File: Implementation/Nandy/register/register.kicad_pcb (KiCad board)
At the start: 2 copper layers, 57.1 x 95.2 mm, 47 parts, among them J1 Conn_02x06_Odd_Even, J2 Conn_02x06_Odd_Even, J3 Conn_01x04_Male

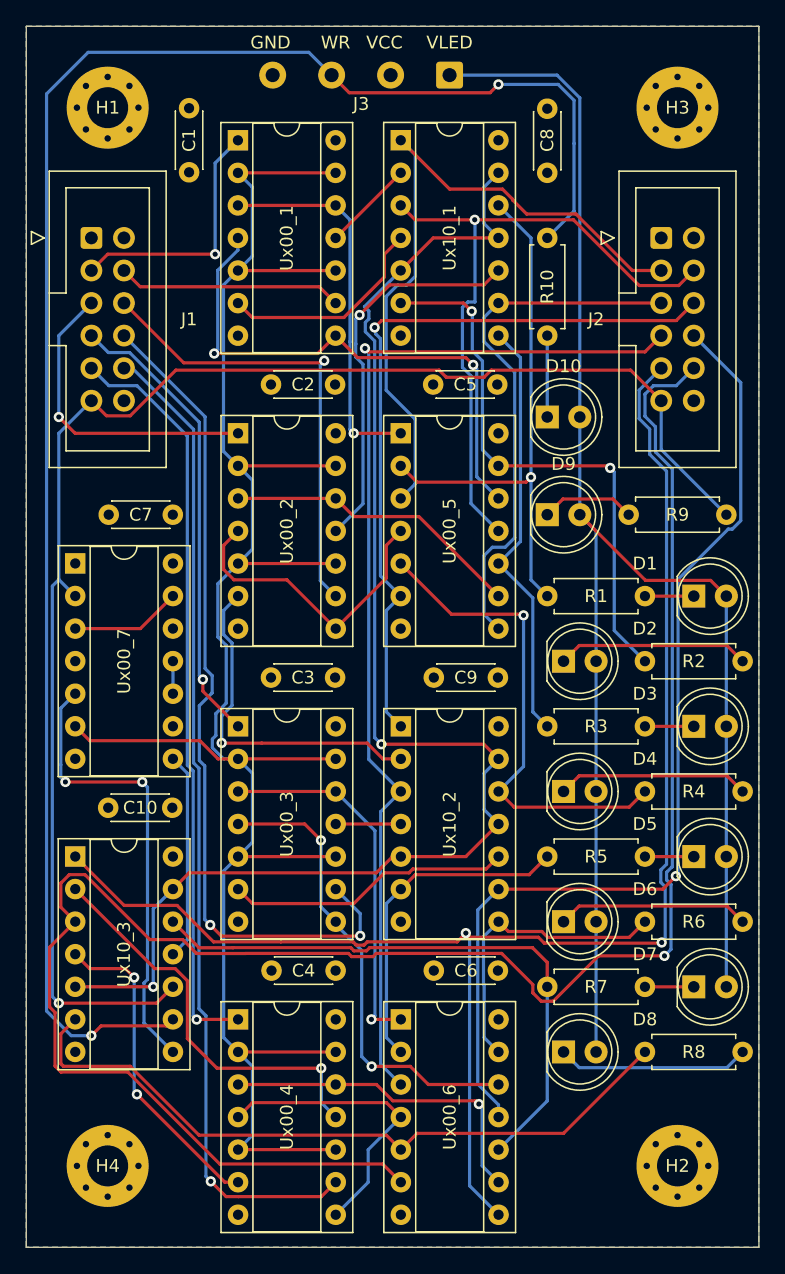
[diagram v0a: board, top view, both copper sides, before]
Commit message: Reworked Makefile with kikit
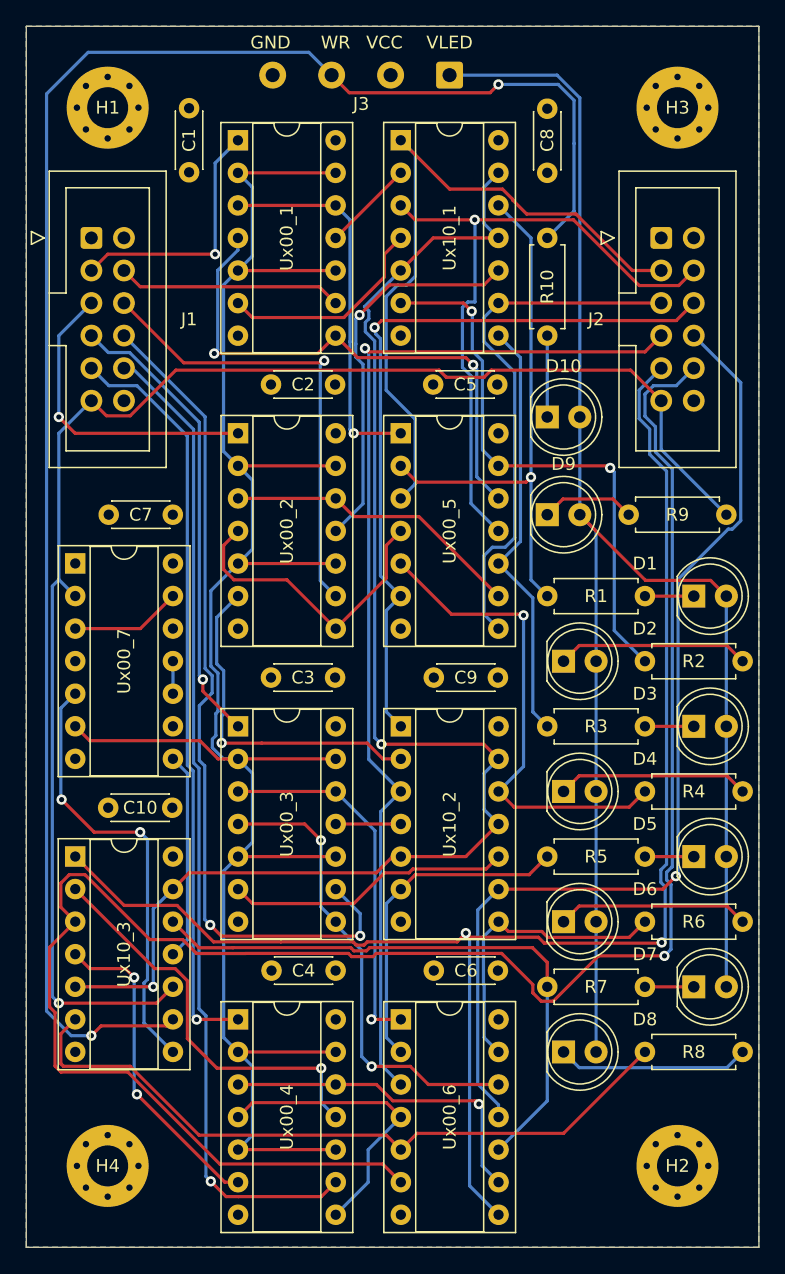
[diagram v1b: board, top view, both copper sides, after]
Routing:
- net /NTICK: track 35.8 -> 34.4 mm
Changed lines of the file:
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@@
       (plotinvisibletext false)
       (sketchpadsonfab false)
-      (subtractmaskfromsilk false)
+      (subtractmaskfromsilk true)
       (outputformat 1)
       (mirror false)
-      (drillshape 1)
+      (drillshape 0)
       (scaleselection 1)
       (outputdirectory "")
@@
     (fp_circle (center 13.8 0) (end 14.85 0)
       (stroke (width 0.1) (type solid)) (fill none) (layer "F.Fab"))
-    (pad "1" thru_hole roundrect (at 0 0 180) (size 2.1 2.1) (drill 1.1) (layers "*.Cu" "*.Mask") (roundrect_rratio 0.119048)
+    (pad "1" thru_hole roundrect (at 0 0 180) (size 2.1 2.1) (drill 1.1) (layers "*.Cu" "*.Mask") (roundrect_rratio 0.1190480952)
       (net 4 "+5VL") (pinfunction "Pin_1") (pintype "passive"))
     (pad "2" thru_hole circle (at 4.6 0 180) (size 2.1 2.1) (drill 1.1) (layers "*.Cu" "*.Mask")
@@
     (fp_line (start 5.72 17.8) (end -3.18 17.8)
       (stroke (width 0.1) (type solid)) (layer "F.Fab"))
-    (pad "1" thru_hole roundrect (at 0 0) (size 1.7 1.7) (drill 1) (layers "*.Cu" "*.Mask") (roundrect_rratio 0.147059)
+    (pad "1" thru_hole roundrect (at 0 0) (size 1.7 1.7) (drill 1) (layers "*.Cu" "*.Mask") (roundrect_rratio 0.1470588235)
       (net 1 "+5V") (pinfunction "Pin_1") (pintype "passive"))
     (pad "2" thru_hole circle (at 2.54 0) (size 1.7 1.7) (drill 1) (layers "*.Cu" "*.Mask")
@@
     (fp_line (start 5.72 17.8) (end -3.18 17.8)
       (stroke (width 0.1) (type solid)) (layer "F.Fab"))
-    (pad "1" thru_hole roundrect (at 0 0) (size 1.7 1.7) (drill 1) (layers "*.Cu" "*.Mask") (roundrect_rratio 0.147059)
+    (pad "1" thru_hole roundrect (at 0 0) (size 1.7 1.7) (drill 1) (layers "*.Cu" "*.Mask") (roundrect_rratio 0.1470588235)
       (net 1 "+5V") (pinfunction "Pin_1") (pintype "passive"))
     (pad "2" thru_hole circle (at 2.54 0) (size 1.7 1.7) (drill 1) (layers "*.Cu" "*.Mask")
@@
   (segment (start 69.228489 41.769511) (end 72.39 38.608) (width 0.25) (layer "F.Cu") (net 34))
   (segment (start 72.39 38.608) (end 72.39 36.83) (width 0.25) (layer "F.Cu") (net 34))
-  (segment (start 47.5 78) (end 53.5 78) (width 0.25) (layer "F.Cu") (net 35))
-  (via (at 53.5 78) (size 0.8) (drill 0.4) (layers "F.Cu" "B.Cu") (net 35))
-  (via (at 47.5 78) (size 0.8) (drill 0.4) (layers "F.Cu" "B.Cu") (net 35))
-  (segment (start 53.5 78) (end 53.90648 78.40648) (width 0.25) (layer "B.Cu") (net 35))
-  (segment (start 53.631489 93.679897) (end 53.631489 96.796489) (width 0.25) (layer "B.Cu") (net 35))
-  (segment (start 47.145489 76.660789) (end 47.145489 72.239511) (width 0.25) (layer "B.Cu") (net 35))
-  (segment (start 53.90648 78.40648) (end 53.90648 93.404906) (width 0.25) (layer "B.Cu") (net 35))
+  (segment (start 53.34 81.915) (end 49.7465 81.915) (width 0.25) (layer "F.Cu") (net 35))
+  (segment (start 49.7465 81.915) (end 47.2065 79.375) (width 0.25) (layer "F.Cu") (net 35))
+  (via (at 53.34 81.915) (size 0.8) (drill 0.4) (layers "F.Cu" "B.Cu") (net 35))
+  (via (at 47.2065 79.375) (size 0.8) (drill 0.4) (layers "F.Cu" "B.Cu") (net 35))
+  (segment (start 47.2065 79.375) (end 47.145489 79.313989) (width 0.25) (layer "B.Cu") (net 35))
+  (segment (start 53.34 81.915) (end 53.90648 82.48148) (width 0.25) (layer "B.Cu") (net 35))
   (segment (start 53.90648 93.404906) (end 53.631489 93.679897) (width 0.25) (layer "B.Cu") (net 35))
-  (segment (start 47.145489 77.645489) (end 47.5 78) (width 0.25) (layer "B.Cu") (net 35))
   (segment (start 53.631489 96.796489) (end 55.89 99.055) (width 0.25) (layer "B.Cu") (net 35))
+  (segment (start 47.145489 79.313989) (end 47.145489 72.239511) (width 0.25) (layer "B.Cu") (net 35))
+  (segment (start 53.631489 93.679897) (end 53.631489 96.796489) (width 0.25) (layer "B.Cu") (net 35))
+  (segment (start 53.90648 82.48148) (end 53.90648 93.404906) (width 0.25) (layer "B.Cu") (net 35))
   (segment (start 47.145489 72.239511) (end 48.27 71.115) (width 0.25) (layer "B.Cu") (net 35))
-  (segment (start 47.145489 76.660789) (end 47.145489 77.645489) (width 0.25) (layer "B.Cu") (net 35))
   (segment (start 55.89 91.435) (end 57.023 90.302) (width 0.25) (layer "B.Cu") (net 36))
   (segment (start 57.023 90.302) (end 57.023 77.328) (width 0.25) (layer "B.Cu") (net 36))
@@
   (segment (start 62.094511 100.184511) (end 60.97 99.06) (width 0.25) (layer "B.Cu") (net 39))
   (segment (start 62.094511 54.464511) (end 60.97 53.34) (width 0.25) (layer "B.Cu") (net 39))
-  (segment (start 58.965489 75.326859) (end 58.965489 74.655297) (width 0.25) (layer "B.Cu") (net 39))
   (segment (start 62.094511 82.695489) (end 62.094511 77.324511) (width 0.25) (layer "B.Cu") (net 39))
-  (segment (start 58.965489 74.655297) (end 59.24048 74.380306) (width 0.25) (layer "B.Cu") (net 39))
+  (segment (start 58.84904 68.96353) (end 58.84904 63.08096) (width 0.25) (layer "B.Cu") (net 39))
+  (segment (start 59.83863 76.2) (end 58.965489 75.326859) (width 0.25) (layer "B.Cu") (net 39))
   (segment (start 59.835489 39.229511) (end 59.835489 52.205489) (width 0.25) (layer "B.Cu") (net 39))
-  (segment (start 60.05048 71.849292) (end 60.05048 67.346498) (width 0.25) (layer "B.Cu") (net 39))
-  (segment (start 59.395969 66.691986) (end 59.395969 62.534031) (width 0.25) (layer "B.Cu") (net 39))
   (segment (start 60.97 106.68) (end 62.094511 105.555489) (width 0.25) (layer "B.Cu") (net 39))
   (segment (start 60.97 83.82) (end 62.094511 82.695489) (width 0.25) (layer "B.Cu") (net 39))
   (segment (start 60.96 38.105) (end 59.835489 39.229511) (width 0.25) (layer "B.Cu") (net 39))
   (segment (start 59.845489 84.944511) (end 60.97 83.82) (width 0.25) (layer "B.Cu") (net 39))
-  (segment (start 60.97 76.2) (end 59.83863 76.2) (width 0.25) (layer "B.Cu") (net 39))
   (segment (start 60.96 38.105) (end 62.084511 36.980489) (width 0.25) (layer "B.Cu") (net 39))
-  (segment (start 59.24048 72.659292) (end 60.05048 71.849292) (width 0.25) (layer "B.Cu") (net 39))
   (segment (start 62.094511 77.324511) (end 60.97 76.2) (width 0.25) (layer "B.Cu") (net 39))
   (segment (start 62.084511 36.980489) (end 62.084511 31.609511) (width 0.25) (layer "B.Cu") (net 39))
   (segment (start 62.094511 59.835489) (end 62.094511 54.464511) (width 0.25) (layer "B.Cu") (net 39))
+  (segment (start 58.965489 74.655297) (end 59.24048 74.380306) (width 0.25) (layer "B.Cu") (net 39))
+  (segment (start 59.24048 72.659292) (end 59.399011 72.500761) (width 0.25) (layer "B.Cu") (net 39))
   (segment (start 59.845489 97.935489) (end 59.845489 84.944511) (width 0.25) (layer "B.Cu") (net 39))
+  (segment (start 59.399011 72.500761) (end 59.399011 69.513501) (width 0.25) (layer "B.Cu") (net 39))
   (segment (start 62.094511 105.555489) (end 62.094511 100.184511) (width 0.25) (layer "B.Cu") (net 39))
-  (segment (start 59.24048 74.380306) (end 59.24048 72.659292) (width 0.25) (layer "B.Cu") (net 39))
   (segment (start 60.97 60.96) (end 62.094511 59.835489) (width 0.25) (layer "B.Cu") (net 39))
-  (segment (start 60.05048 67.346498) (end 59.395969 66.691986) (width 0.25) (layer "B.Cu") (net 39))
+  (segment (start 58.84904 63.08096) (end 60.97 60.96) (width 0.25) (layer "B.Cu") (net 39))
+  (segment (start 59.399011 69.513501) (end 58.84904 68.96353) (width 0.25) (layer "B.Cu") (net 39))
+  (segment (start 58.965489 75.326859) (end 58.965489 74.655297) (width 0.25) (layer "B.Cu") (net 39))
   (segment (start 62.084511 31.609511) (end 60.96 30.485) (width 0.25) (layer "B.Cu") (net 39))
-  (segment (start 59.83863 76.2) (end 58.965489 75.326859) (width 0.25) (layer "B.Cu") (net 39))
   (segment (start 60.97 99.06) (end 59.845489 97.935489) (width 0.25) (layer "B.Cu") (net 39))
+  (segment (start 60.97 76.2) (end 59.83863 76.2) (width 0.25) (layer "B.Cu") (net 39))
   (segment (start 59.835489 52.205489) (end 60.97 53.34) (width 0.25) (layer "B.Cu") (net 39))
-  (segment (start 59.395969 62.534031) (end 60.97 60.96) (width 0.25) (layer "B.Cu") (net 39))
+  (segment (start 59.24048 74.380306) (end 59.24048 72.659292) (width 0.25) (layer "B.Cu") (net 39))
   (segment (start 55.89 68.575) (end 55.89 71.115) (width 0.25) (layer "B.Cu") (net 40))
   (segment (start 68.58 33.025) (end 60.96 33.025) (width 0.25) (layer "F.Cu") (net 41))
@@
   (segment (start 71.036552 74.968866) (end 62.819011 74.968866) (width 0.25) (layer "F.Cu") (net 45))
   (via (at 59.69 74.9554) (size 0.8) (drill 0.4) (layers "F.Cu" "B.Cu") (net 45))
-  (segment (start 60.5 67.1603) (end 59.845489 66.505789) (width 0.25) (layer "B.Cu") (net 45))
-  (segment (start 59.69 74.9554) (end 59.69 72.845489) (width 0.25) (layer "B.Cu") (net 45))
-  (segment (start 59.69 72.845489) (end 60.5 72.035489) (width 0.25) (layer "B.Cu") (net 45))
-  (segment (start 59.845489 66.505789) (end 59.845489 64.624511) (width 0.25) (layer "B.Cu") (net 45))
-  (segment (start 60.5 72.035489) (end 60.5 67.1603) (width 0.25) (layer "B.Cu") (net 45))
-  (segment (start 59.845489 64.624511) (end 60.97 63.5) (width 0.25) (layer "B.Cu") (net 45))
+  (segment (start 59.29904 65.17096) (end 60.97 63.5) (width 0.25) (layer "B.Cu") (net 45))
+  (segment (start 59.29904 68.777134) (end 59.29904 65.17096) (width 0.25) (layer "B.Cu") (net 45))
+  (segment (start 59.69 74.9554) (end 59.69 72.846168) (width 0.25) (layer "B.Cu") (net 45))
+  (segment (start 59.69 72.846168) (end 59.849011 72.687157) (width 0.25) (layer "B.Cu") (net 45))
+  (segment (start 59.849011 69.327105) (end 59.29904 68.777134) (width 0.25) (layer "B.Cu") (net 45))
+  (segment (start 59.849011 72.687157) (end 59.849011 69.327105) (width 0.25) (layer "B.Cu") (net 45))
   (segment (start 68.59 81.28) (end 73.67 81.28) (width 0.25) (layer "F.Cu") (net 46))
   (segment (start 71.371469 96.52) (end 73.67 96.52) (width 0.25) (layer "F.Cu") (net 47))
